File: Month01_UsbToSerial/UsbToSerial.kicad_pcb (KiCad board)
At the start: 2 copper layers, 34.5 x 20.3 mm, 14 parts, among them J1 USB_B_Micro, J2 Conn_01x08_Male, J3 Conn_01x08_Male, U1 FT232RL

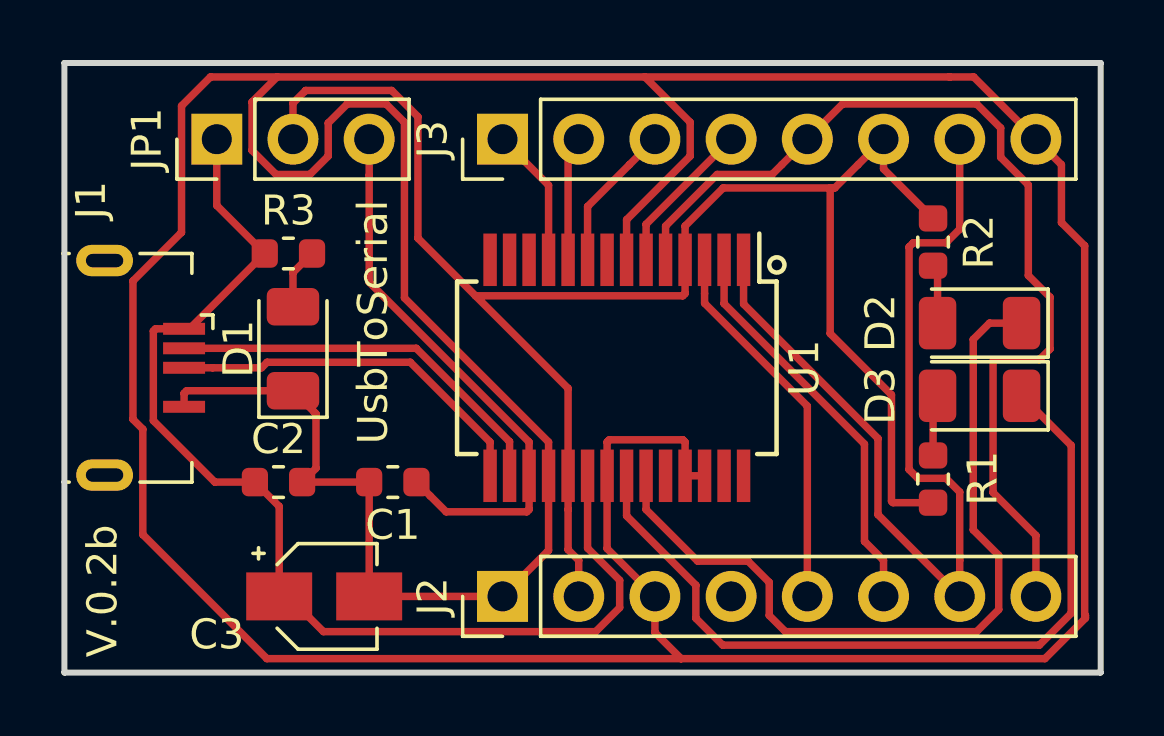
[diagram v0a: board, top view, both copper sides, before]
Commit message: #3 added via and track to back of board for DTR pin
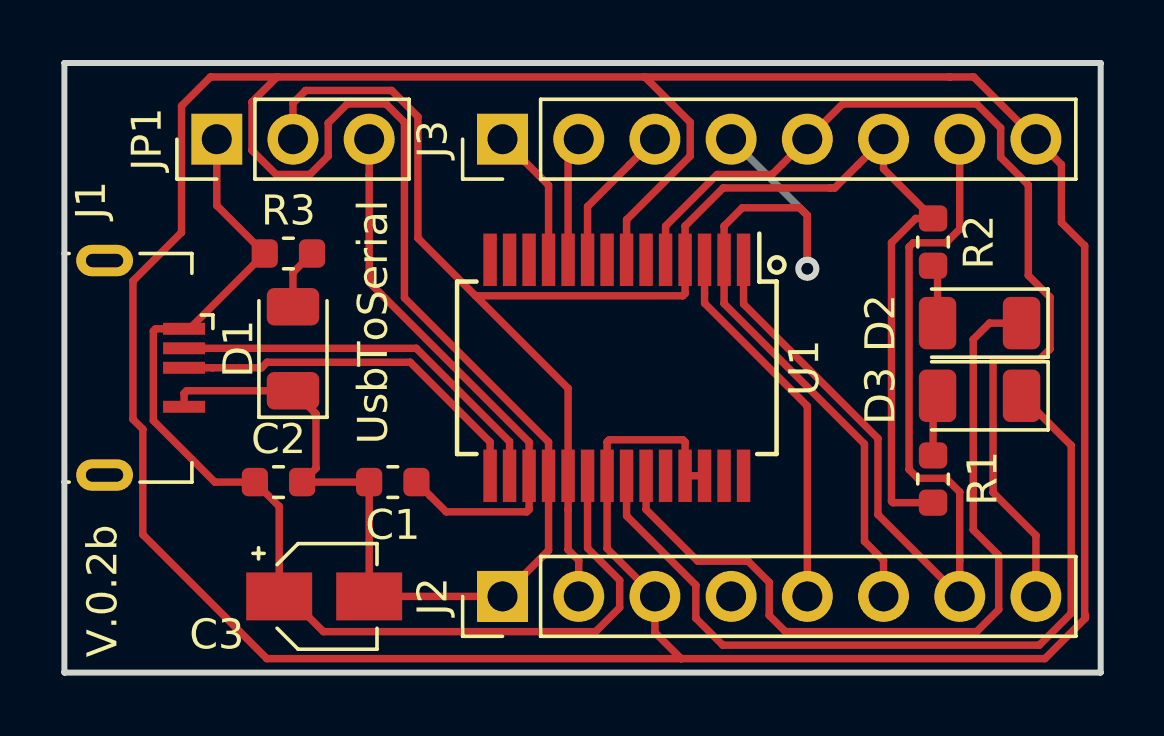
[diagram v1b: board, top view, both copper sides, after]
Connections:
- J3 pad 4: RI -> DTR
- U1 pad 6: RI -> Net-(U1-Pad6)
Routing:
- net DTR: track 13.4 -> 24.8 mm, vias 0 -> 1
- net RI: track 5.19 -> 0.00 mm
- net PWR: track 57.2 -> 56.3 mm
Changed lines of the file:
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@@
     (thickness 1.6)
     (drawings 39)
-    (tracks 202)
+    (tracks 208)
     (zones 0)
     (modules 14)
@@
   (net 21 TX0)
   (net 22 RTS)
-  (net 23 RI)
-  (net 24 DCR)
-  (net 25 DCD)
-  (net 26 "Net-(J2-Pad4)")
+  (net 23 DCR)
+  (net 24 DCD)
+  (net 25 "Net-(J2-Pad4)")
+  (net 26 "Net-(U1-Pad6)")
   (net_class Default "This is the default net class."
     (clearance 0.2)
@@
     (add_net "Net-(U1-Pad27)")
     (add_net "Net-(U1-Pad28)")
+    (add_net "Net-(U1-Pad6)")
     (add_net PWR)
-    (add_net RI)
     (add_net RTS)
     (add_net RXI)
@@
       (net 18 RXI))
     (pad 6 smd rect (at -3.6 -0.975 270) (size 1.75 0.45) (layers F.Cu F.Paste F.Mask)
-      (net 23 RI))
+      (net 26 "Net-(U1-Pad6)"))
     (pad 7 smd rect (at -3.6 -0.325 270) (size 1.75 0.45) (layers F.Cu F.Paste F.Mask)
       (net 2 GNDREF))
     (pad 8 smd rect (at -3.6 0.325 270) (size 1.75 0.45) (layers F.Cu F.Paste F.Mask))
     (pad 9 smd rect (at -3.6 0.975 270) (size 1.75 0.45) (layers F.Cu F.Paste F.Mask)
-      (net 24 DCR))
+      (net 23 DCR))
     (pad 10 smd rect (at -3.6 1.625 270) (size 1.75 0.45) (layers F.Cu F.Paste F.Mask)
-      (net 25 DCD))
+      (net 24 DCD))
     (pad 11 smd rect (at -3.6 2.275 270) (size 1.75 0.45) (layers F.Cu F.Paste F.Mask)
       (net 16 CTS))
@@
       (net 22 RTS))
     (pad 4 thru_hole oval (at 0 7.62 90) (size 1.7 1.7) (drill 1) (layers *.Cu *.Mask)
-      (net 26 "Net-(J2-Pad4)"))
+      (net 25 "Net-(J2-Pad4)"))
     (pad 3 thru_hole oval (at 0 5.08 90) (size 1.7 1.7) (drill 1) (layers *.Cu *.Mask)
       (net 2 GNDREF))
@@
       (net 16 CTS))
     (pad 2 thru_hole oval (at 0 2.54 90) (size 1.7 1.7) (drill 1) (layers *.Cu *.Mask)
-      (net 25 DCD))
+      (net 24 DCD))
     (pad 3 thru_hole oval (at 0 5.08 90) (size 1.7 1.7) (drill 1) (layers *.Cu *.Mask)
-      (net 24 DCR))
+      (net 23 DCR))
     (pad 4 thru_hole oval (at 0 7.62 90) (size 1.7 1.7) (drill 1) (layers *.Cu *.Mask)
-      (net 23 RI))
+      (net 19 DTR))
     (pad 5 thru_hole oval (at 0 10.16 90) (size 1.7 1.7) (drill 1) (layers *.Cu *.Mask)
       (net 18 RXI))
@@
   (gr_line (start 112.649 69.85) (end 112.649 90.17) (layer Edge.Cuts) (width 0.2))
   (gr_line (start 78.105 69.85) (end 112.649 69.85) (layer Edge.Cuts) (width 0.2))
+  (via (at 102.87 76.708) (size 0.8) (drill 0.4) (layers F.Cu B.Cu) (net 19))
   (segment (start 82.275 78.71) (end 82.095 78.71) (width 0.25) (layer F.Cu) (net 1))
   (segment (start 84.785 76.2) (end 82.275 78.71) (width 0.25) (layer F.Cu) (net 1))
@@
   (segment (start 105.41 73.3805) (end 105.41 72.39) (width 0.25) (layer F.Cu) (net 17))
   (segment (start 107.061 75.0315) (end 105.41 73.3805) (width 0.25) (layer F.Cu) (net 17))
-  (segment (start 107.061 84.506) (end 105.72602 84.506) (width 0.25) (layer F.Cu) (net 17))
-  (segment (start 105.67502 84.455) (end 105.67502 80.91002) (width 0.25) (layer F.Cu) (net 17))
-  (segment (start 105.72602 84.506) (end 105.67502 84.455) (width 0.25) (layer F.Cu) (net 17))
-  (segment (start 103.632 78.867) (end 103.632 74.015011) (width 0.25) (layer F.Cu) (net 17))
-  (segment (start 105.67502 80.91002) (end 103.632 78.867) (width 0.25) (layer F.Cu) (net 17))
   (segment (start 100.064989 74.015011) (end 103.632 74.015011) (width 0.25) (layer F.Cu) (net 17))
   (segment (start 103.632 74.015011) (end 103.784989 74.015011) (width 0.25) (layer F.Cu) (net 17))
+  (segment (start 106.486 75.0315) (end 107.061 75.0315) (width 0.25) (layer F.Cu) (net 17))
+  (segment (start 105.67502 75.84248) (end 106.486 75.0315) (width 0.25) (layer F.Cu) (net 17))
+  (segment (start 105.67502 84.455) (end 105.67502 75.84248) (width 0.25) (layer F.Cu) (net 17))
+  (segment (start 105.72602 84.506) (end 105.67502 84.455) (width 0.25) (layer F.Cu) (net 17))
+  (segment (start 107.061 84.506) (end 105.72602 84.506) (width 0.25) (layer F.Cu) (net 17))
   (segment (start 102.020001 73.239999) (end 102.87 72.39) (width 0.25) (layer F.Cu) (net 18))
   (segment (start 101.694999 73.565001) (end 102.020001 73.239999) (width 0.25) (layer F.Cu) (net 18))
@@
   (segment (start 100.095 77.87141) (end 104.775 82.55141) (width 0.25) (layer F.Cu) (net 19))
   (segment (start 100.095 76.41) (end 100.095 77.87141) (width 0.25) (layer F.Cu) (net 19))
+  (segment (start 102.87 74.93) (end 102.87 76.708) (width 0.25) (layer F.Cu) (net 19))
+  (segment (start 102.616 74.676) (end 102.87 74.93) (width 0.25) (layer F.Cu) (net 19))
+  (segment (start 100.704 74.676) (end 102.616 74.676) (width 0.25) (layer F.Cu) (net 19))
+  (segment (start 100.095 76.41) (end 100.095 75.285) (width 0.25) (layer F.Cu) (net 19))
+  (segment (start 100.095 75.285) (end 100.704 74.676) (width 0.25) (layer F.Cu) (net 19))
+  (segment (start 102.87 74.93) (end 100.33 72.39) (width 0.25) (layer B.Cu) (net 19))
+  (segment (start 102.87 76.708) (end 102.87 74.93) (width 0.25) (layer B.Cu) (net 19))
   (segment (start 88.265 73.592081) (end 88.265 72.39) (width 0.25) (layer F.Cu) (net 20))
   (segment (start 88.265 77.155) (end 88.265 73.592081) (width 0.25) (layer F.Cu) (net 20))
@@
   (segment (start 102.87 81.28282) (end 99.445 77.85782) (width 0.25) (layer F.Cu) (net 22))
   (segment (start 102.87 87.63) (end 102.87 81.28282) (width 0.25) (layer F.Cu) (net 22))
-  (segment (start 97.495 75.225) (end 100.33 72.39) (width 0.25) (layer F.Cu) (net 23))
-  (segment (start 97.495 76.41) (end 97.495 75.225) (width 0.25) (layer F.Cu) (net 23))
-  (segment (start 96.940001 73.239999) (end 97.79 72.39) (width 0.25) (layer F.Cu) (net 24))
-  (segment (start 95.545 74.635) (end 96.940001 73.239999) (width 0.25) (layer F.Cu) (net 24))
-  (segment (start 95.545 76.41) (end 95.545 74.635) (width 0.25) (layer F.Cu) (net 24))
-  (segment (start 94.895 72.745) (end 95.25 72.39) (width 0.25) (layer F.Cu) (net 25))
-  (segment (start 94.895 76.41) (end 94.895 72.745) (width 0.25) (layer F.Cu) (net 25))
+  (segment (start 96.940001 73.239999) (end 97.79 72.39) (width 0.25) (layer F.Cu) (net 23))
+  (segment (start 95.545 74.635) (end 96.940001 73.239999) (width 0.25) (layer F.Cu) (net 23))
+  (segment (start 95.545 76.41) (end 95.545 74.635) (width 0.25) (layer F.Cu) (net 23))
+  (segment (start 94.895 72.745) (end 95.25 72.39) (width 0.25) (layer F.Cu) (net 24))
+  (segment (start 94.895 76.41) (end 94.895 72.745) (width 0.25) (layer F.Cu) (net 24))
 )
